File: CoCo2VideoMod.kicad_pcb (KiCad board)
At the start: 2 copper layers, 38 x 50 mm, 36 parts, among them J1 20261043, J2 to PCB, J3 Video, Q1 BC547, Q2 BC557, Q3 BC547, Q4 BC557, Q5 BC547, U1 MC1372P

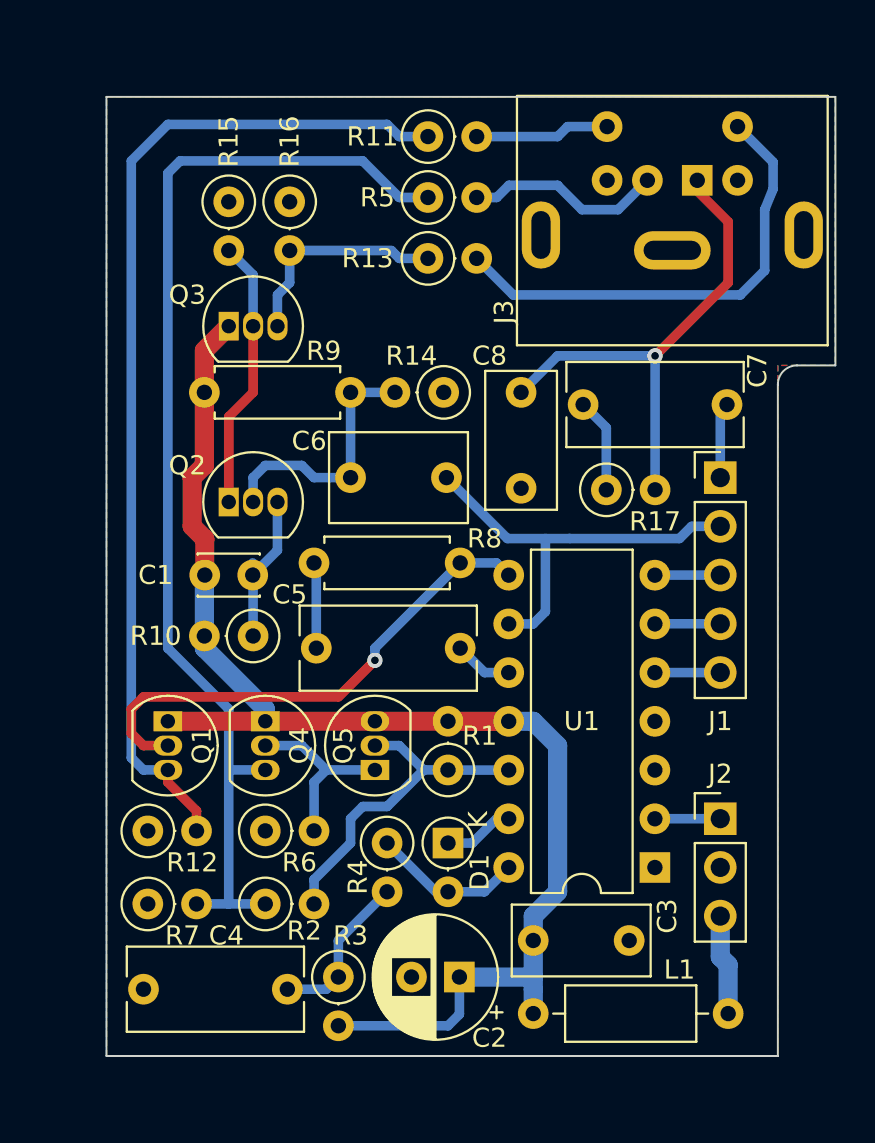
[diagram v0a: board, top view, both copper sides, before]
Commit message: increased distance components to PCB edge
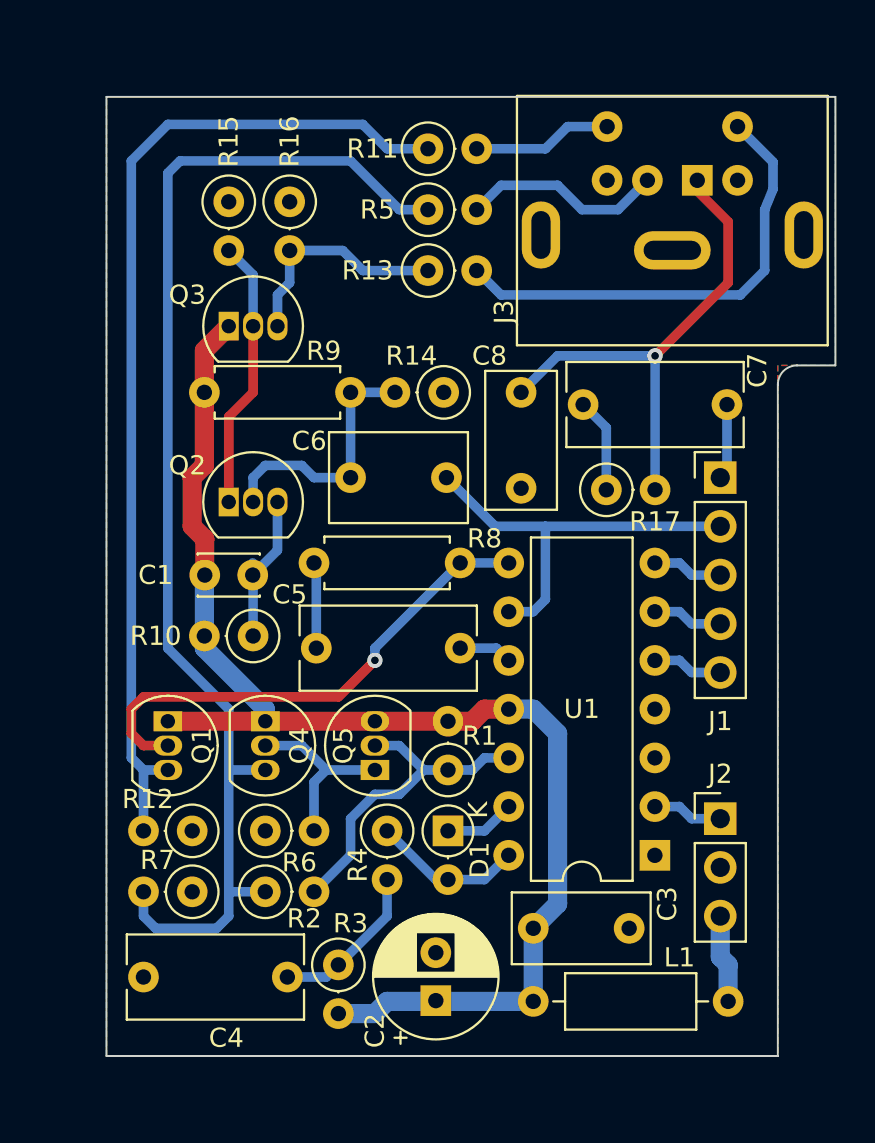
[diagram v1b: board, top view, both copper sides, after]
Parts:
- moved R7 2.40 mm to (204.5, 91.4), turned to 180 degrees
- moved R12 2.31 mm to (204.5, 88.3), turned to 180 degrees
- moved C2 1.74 mm to (217.2, 97.1), turned to 90 degrees
- moved C3 0.64 mm to (222.2, 93.3)
- moved D1 0.64 mm to (217.8, 88.3)
- moved L1 0.64 mm to (232.4, 97.2)
- moved R2 0.64 mm to (208.3, 91.4)
- moved R3 0.64 mm to (212.1, 95.2)
- moved R4 0.64 mm to (214.6, 88.3)
- moved R5 0.64 mm to (216.8, 55.9)
- moved R11 0.63 mm to (216.8, 52.7)
- moved R13 0.63 mm to (216.8, 59.1)
- moved C4 0.63 mm to (201.9, 95.9)
- moved U1 0.63 mm to (228.6, 89.5)
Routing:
- net Net-(Q5-E): track 59.5 -> 65.0 mm
- net +5V: track 70.7 -> 69.0 mm
- net /+5V in: track 5.25 -> 4.61 mm
- net /Luma: track 21.8 -> 21.3 mm

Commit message: production files JLC, production complete
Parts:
- moved J3 1.30 mm to (229.5, 54.4)

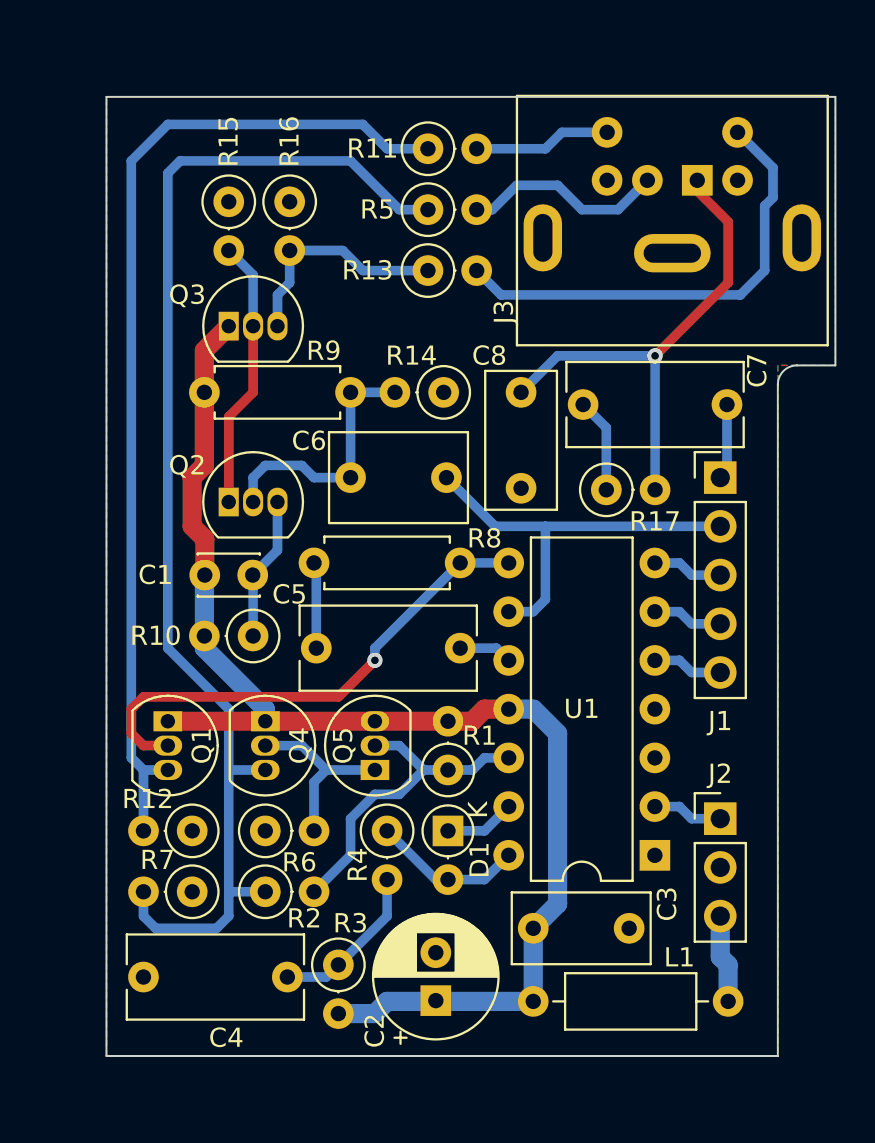
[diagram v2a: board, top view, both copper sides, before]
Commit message: rotated connector, added GND pins
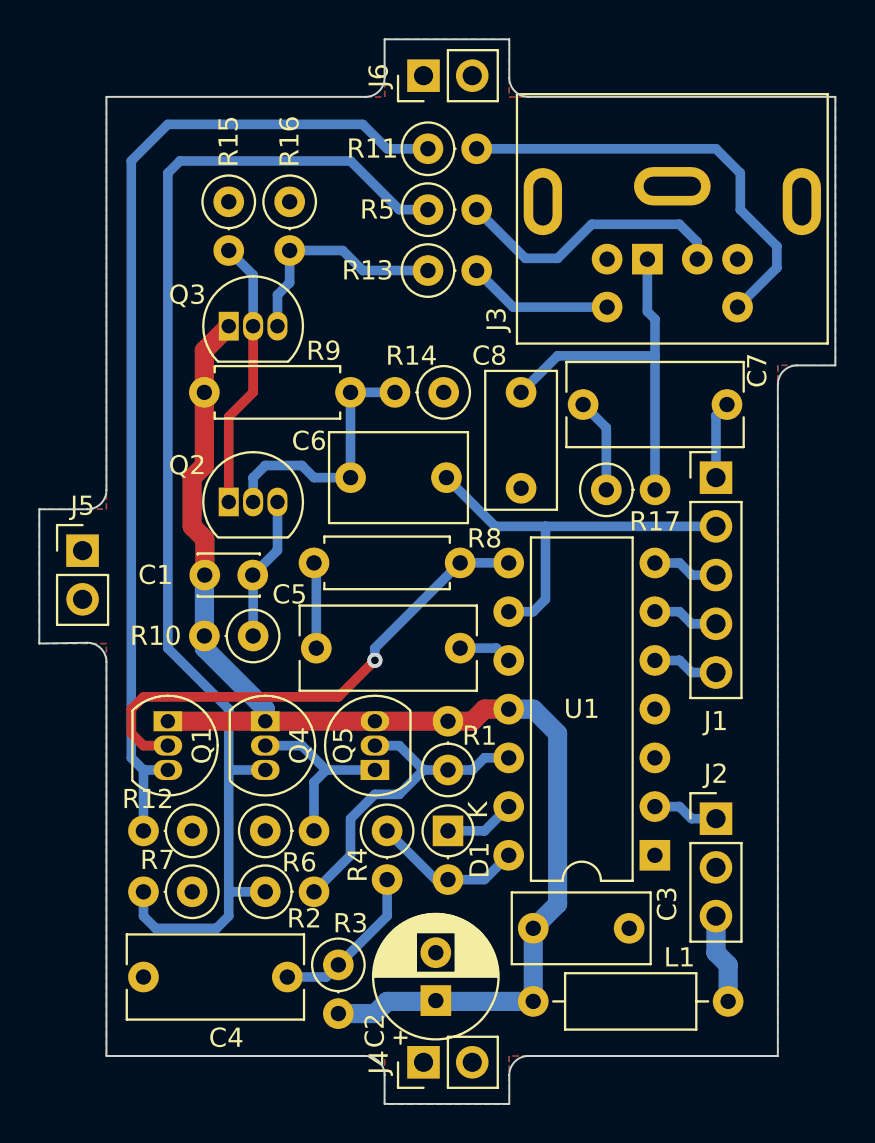
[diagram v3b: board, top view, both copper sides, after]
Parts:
- added J4: GND_S, Connector_PinHeader_2.54mm:PinHeader_1x02_P2.54mm_Vertical, F.Cu at (216.5, 100.3)
- added J5: GND_W, Connector_PinHeader_2.54mm:PinHeader_1x02_P2.54mm_Vertical, F.Cu at (198.8, 73.7)
- added J6: GND_N, Connector_PinHeader_2.54mm:PinHeader_1x02_P2.54mm_Vertical, F.Cu at (216.5, 48.9)
- moved J3 4.11 mm to (229.5, 58.5), turned to 180 degrees
- moved J1 0.22 mm to (231.8, 69.8)
- moved J2 0.22 mm to (231.8, 87.6)
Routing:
- net /Luma_out: track 24.2 -> 7.59 mm
- net /Chroma_out: track 7.15 -> 22.9 mm
- net /Audio out: track 26.7 -> 20.0 mm, vias 1 -> 0
- net /Composite_out: track 10.6 -> 14.6 mm
- net GND: track 2.11 -> 1.11 mm
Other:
- board size 38 x 50 mm -> 41.5 x 55.5 mm

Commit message: adjusted GND pin position, added PCB description to silk screen, started README
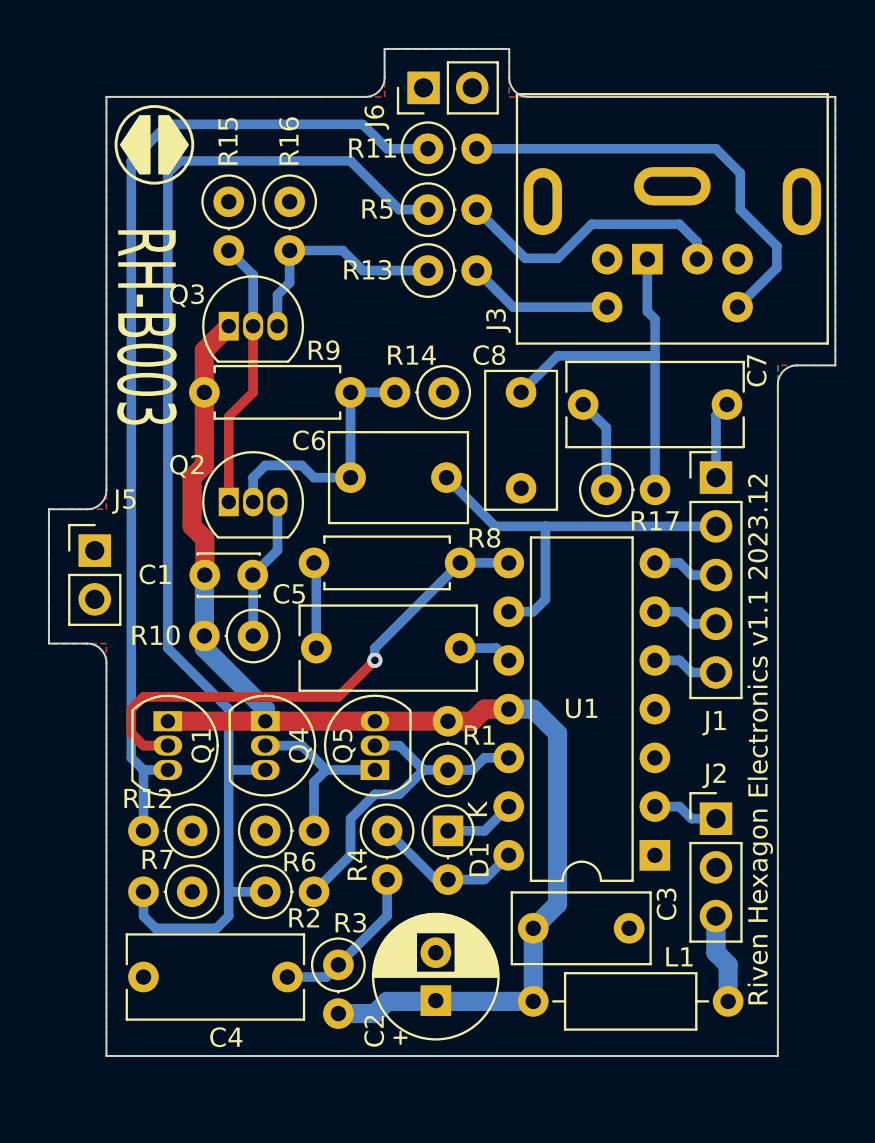
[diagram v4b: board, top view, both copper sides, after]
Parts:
- removed J4: GND_S, Connector_PinHeader_2.54mm:PinHeader_1x02_P2.54mm_Vertical
- moved J6 0.63 mm to (216.5, 49.5)
- moved J5 0.63 mm to (199.4, 73.7)
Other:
- board size 41.5 x 55.5 mm -> 41 x 52.5 mm
- board text added: "RH-B003"
- board text added: "Riven Hexagon Electronics v1.1 2023.12"
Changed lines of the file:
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@@
   )
   (footprint "Connector_PinHeader_2.54mm:PinHeader_1x02_P2.54mm_Vertical" (layer "F.Cu")
-    (at 216.53 48.895 90)
+    (at 216.53 49.53 90)
     (descr "Through hole straight pin header, 1x02, 2.54mm pitch, single row")
     (tags "Through hole pin header THT 1x02 2.54mm single row")
@@
     (property "ki_keywords" "connector")
     (attr through_hole)
-    (fp_text reference "J6" (at 0 -2.33 90) (layer "F.SilkS")
+    (fp_text reference "J6" (at -1.47 -2.53 90) (layer "F.SilkS")
         (effects (font (size 1 1) (thickness 0.15)))
     )
@@
       (net 3 "GND") (pintype "passive"))
     (model "${KICAD6_3DMODEL_DIR}/Capacitor_THT.3dshapes/CP_Radial_D6.3mm_P2.50mm.wrl"
-      (offset (xyz 0 0 0))
-      (scale (xyz 1 1 1))
-      (rotate (xyz 0 0 0))
-    )
-  )
-  (footprint "Connector_PinHeader_2.54mm:PinHeader_1x02_P2.54mm_Vertical" (layer "F.Cu")
-    (at 216.53 100.33 90)
-    (descr "Through hole straight pin header, 1x02, 2.54mm pitch, single row")
-    (tags "Through hole pin header THT 1x02 2.54mm single row")
-    (property "Sheetfile" "CoCo2VideoMod.kicad_sch")
-    (property "Sheetname" "")
-    (property "ki_description" "Generic connector, single row, 01x02, script generated (kicad-library-utils/schlib/autogen/connector/)")
-    (property "ki_keywords" "connector")
-    (attr through_hole)
-    (fp_text reference "J4" (at 0 -2.33 90) (layer "F.SilkS")
-        (effects (font (size 1 1) (thickness 0.15)))
-    )
-    (fp_text value "GND_S" (at 0 4.87 90) (layer "F.Fab")
-        (effects (font (size 1 1) (thickness 0.15)))
-    )
-    (fp_text user "${REFERENCE}" (at 0 1.27) (layer "F.Fab")
-        (effects (font (size 1 1) (thickness 0.15)))
-    )
-    (fp_line (start -1.33 -1.33) (end 0 -1.33)
-      (stroke (width 0.12) (type solid)) (layer "F.SilkS"))
-    (fp_line (start -1.33 0) (end -1.33 -1.33)
-      (stroke (width 0.12) (type solid)) (layer "F.SilkS"))
-    (fp_line (start -1.33 1.27) (end -1.33 3.87)
-      (stroke (width 0.12) (type solid)) (layer "F.SilkS"))
-    (fp_line (start -1.33 1.27) (end 1.33 1.27)
-      (stroke (width 0.12) (type solid)) (layer "F.SilkS"))
-    (fp_line (start -1.33 3.87) (end 1.33 3.87)
-      (stroke (width 0.12) (type solid)) (layer "F.SilkS"))
-    (fp_line (start 1.33 1.27) (end 1.33 3.87)
-      (stroke (width 0.12) (type solid)) (layer "F.SilkS"))
-    (fp_line (start -1.8 -1.8) (end -1.8 4.35)
-      (stroke (width 0.05) (type solid)) (layer "F.CrtYd"))
-    (fp_line (start -1.8 4.35) (end 1.8 4.35)
-      (stroke (width 0.05) (type solid)) (layer "F.CrtYd"))
-    (fp_line (start 1.8 -1.8) (end -1.8 -1.8)
-      (stroke (width 0.05) (type solid)) (layer "F.CrtYd"))
-    (fp_line (start 1.8 4.35) (end 1.8 -1.8)
-      (stroke (width 0.05) (type solid)) (layer "F.CrtYd"))
-    (fp_line (start -1.27 -0.635) (end -0.635 -1.27)
-      (stroke (width 0.1) (type solid)) (layer "F.Fab"))
-    (fp_line (start -1.27 3.81) (end -1.27 -0.635)
-      (stroke (width 0.1) (type solid)) (layer "F.Fab"))
-    (fp_line (start -0.635 -1.27) (end 1.27 -1.27)
-      (stroke (width 0.1) (type solid)) (layer "F.Fab"))
-    (fp_line (start 1.27 -1.27) (end 1.27 3.81)
-      (stroke (width 0.1) (type solid)) (layer "F.Fab"))
-    (fp_line (start 1.27 3.81) (end -1.27 3.81)
-      (stroke (width 0.1) (type solid)) (layer "F.Fab"))
-    (pad "1" thru_hole rect (at 0 0 90) (size 1.7 1.7) (drill 1) (layers "*.Cu" "*.Mask")
-      (net 3 "GND") (pinfunction "Pin_1") (pintype "passive"))
-    (pad "2" thru_hole oval (at 0 2.54 90) (size 1.7 1.7) (drill 1) (layers "*.Cu" "*.Mask")
-      (net 3 "GND") (pinfunction "Pin_2") (pintype "passive"))
-    (model "${KICAD6_3DMODEL_DIR}/Connector_PinHeader_2.54mm.3dshapes/PinHeader_1x02_P2.54mm_Vertical.wrl"
       (offset (xyz 0 0 0))
       (scale (xyz 1 1 1))
@@
   )
   (footprint "Connector_PinHeader_2.54mm:PinHeader_1x02_P2.54mm_Vertical" (layer "F.Cu")
-    (at 198.755 73.655)
+    (at 199.39 73.655)
     (descr "Through hole straight pin header, 1x02, 2.54mm pitch, single row")
     (tags "Through hole pin header THT 1x02 2.54mm single row")
@@
     (property "ki_keywords" "connector")
     (attr through_hole)
-    (fp_text reference "J5" (at 0 -2.33) (layer "F.SilkS")
+    (fp_text reference "J5" (at 1.61 -2.655) (layer "F.SilkS")
         (effects (font (size 1 1) (thickness 0.15)))
     )
@@
     )
   )
-  (gr_line (start 196.5 71.5) (end 196.5 78.5)
+  (gr_poly
+    (pts
+      (xy 201.75 54)
+      (xy 200.75 52.5)
+      (xy 201.75 51)
+      (xy 202.25 51)
+      (xy 202.25 54)
+    )
+    (stroke (width 0.1) (type solid)) (fill solid) (layer "F.SilkS"))
+  (gr_circle (center 202.5 52.5) (end 202.5 54.5)
+    (stroke (width 0.15) (type solid)) (fill none) (layer "F.SilkS"))
+  (gr_poly
+    (pts
+      (xy 203.25 54)
+      (xy 202.75 54)
+      (xy 202.75 51)
+      (xy 203.25 51)
+      (xy 204.25 52.5)
+    )
+    (stroke (width 0.1) (type solid)) (fill solid) (layer "F.SilkS"))
+  (gr_line (start 197 71.5) (end 197 78.5)
     (stroke (width 0.1) (type default)) (layer "Edge.Cuts"))
-  (gr_line (start 221.000001 47) (end 221.000001 48.999999)
+  (gr_line (start 221.000001 47.5) (end 221.000001 49)
     (stroke (width 0.1) (type default)) (layer "Edge.Cuts"))
-  (gr_line (start 200 100) (end 200 79.457107)
-    (stroke (width 0.1) (type default)) (layer "Edge.Cuts"))
-  (gr_arc (start 221 101) (mid 221.292893 100.292893) (end 222 100)
-    (stroke (width 0.1) (type default)) (layer "Edge.Cuts"))
-  (gr_line (start 221 102.5) (end 214.5 102.5)
+  (gr_line (start 200 100) (end 200 79.500007)
     (stroke (width 0.1) (type default)) (layer "Edge.Cuts"))
   (gr_line (start 238 50) (end 222.000001 49.999999)
     (stroke (width 0.1) (type default)) (layer "Edge.Cuts"))
-  (gr_arc (start 199 78.457107) (mid 199.707107 78.75) (end 200 79.457107)
+  (gr_arc (start 222.000001 49.999999) (mid 221.292894 49.707106) (end 221.000001 49)
     (stroke (width 0.1) (type default)) (layer "Edge.Cuts"))
-  (gr_line (start 196.5 78.5) (end 199 78.457107)
+  (gr_line (start 197 78.5) (end 199 78.500007)
     (stroke (width 0.1) (type default)) (layer "Edge.Cuts"))
-  (gr_line (start 214.5 49) (end 214.5 47)
+  (gr_line (start 214.5 49) (end 214.5 47.5)
+    (stroke (width 0.1) (type default)) (layer "Edge.Cuts"))
+  (gr_arc (start 199 78.500007) (mid 199.707104 78.792901) (end 199.999993 79.500007)
     (stroke (width 0.1) (type default)) (layer "Edge.Cuts"))
   (gr_arc (start 235 65) (mid 235.292893 64.292893) (end 236 64)
@@
   (gr_line (start 236 64) (end 238 64)
     (stroke (width 0.1) (type default)) (layer "Edge.Cuts"))
-  (gr_arc (start 213.5 100) (mid 214.207107 100.292893) (end 214.5 101)
+  (gr_line (start 199 71.5) (end 197 71.5)
     (stroke (width 0.1) (type default)) (layer "Edge.Cuts"))
-  (gr_line (start 199 71.5) (end 196.5 71.5)
+  (gr_line (start 235 100) (end 200 100)
     (stroke (width 0.1) (type default)) (layer "Edge.Cuts"))
-  (gr_line (start 235 100) (end 222 100)
+  (gr_line (start 238 64) (end 238 50)
+    (stroke (width 0.1) (type default)) (layer "Edge.Cuts"))
+  (gr_arc (start 200 70.5) (mid 199.707107 71.207107) (end 199 71.5)
     (stroke (width 0.1) (type default)) (layer "Edge.Cuts"))
   (gr_arc (start 214.5 49) (mid 214.207107 49.707107) (end 213.5 50)
     (stroke (width 0.1) (type default)) (layer "Edge.Cuts"))
-  (gr_line (start 214.5 102.5) (end 214.5 101)
-    (stroke (width 0.1) (type default)) (layer "Edge.Cuts"))
-  (gr_line (start 213.5 100) (end 200 100)
-    (stroke (width 0.1) (type default)) (layer "Edge.Cuts"))
-  (gr_line (start 238 64) (end 238 50)
-    (stroke (width 0.1) (type default)) (layer "Edge.Cuts"))
-  (gr_arc (start 222.000001 49.999999) (mid 221.292894 49.707106) (end 221.000001 48.999999)
-    (stroke (width 0.1) (type default)) (layer "Edge.Cuts"))
-  (gr_arc (start 200 70.5) (mid 199.707107 71.207107) (end 199 71.5)
-    (stroke (width 0.1) (type default)) (layer "Edge.Cuts"))
   (gr_line (start 200 50) (end 213.5 50)
     (stroke (width 0.1) (type default)) (layer "Edge.Cuts"))
-  (gr_line (start 221 101) (end 221 102.5)
-    (stroke (width 0.1) (type default)) (layer "Edge.Cuts"))
-  (gr_line (start 214.5 47) (end 221.000001 47)
+  (gr_line (start 214.5 47.5) (end 221.000001 47.5)
     (stroke (width 0.1) (type default)) (layer "Edge.Cuts"))
   (gr_line (start 200 70.5) (end 200 50)
@@
   (gr_line (start 235 100) (end 235 65)
     (stroke (width 0.1) (type default)) (layer "Edge.Cuts"))
+  (gr_text "RH-B003" (at 202 62 270) (layer "F.SilkS")
+    (effects (font (size 3 1.75) (thickness 0.3)))
+  )
+  (gr_text "Riven Hexagon Electronics v1.1 2023.12" (at 234 83.5 90) (layer "F.SilkS")
+    (effects (font (size 1 1) (thickness 0.15)))
+  )
   (gr_text "K" (at 219.964 87.63 90) (layer "F.SilkS")
     (effects (font (size 1 1) (thickness 0.15)) (justify left bottom))
@@
       (pts
         (xy 200 78.5)
-        (xy 196.5 78.5)
-        (xy 196.5 71.5)
+        (xy 197 78.5)
+        (xy 197 71.5)
         (xy 200 71.5)
         (xy 200 50)
         (xy 214.5 50)
-        (xy 214.5 47)
-        (xy 221 47)
+        (xy 214.5 47.5)
+        (xy 221 47.5)
         (xy 221 50)
         (xy 238 50)
@@
         (xy 235 64)
         (xy 235 100)
-        (xy 221 100)
-        (xy 221 102.5)
-        (xy 214.5 102.5)
-        (xy 214.5 100)
         (xy 200 100)
       )
@@
       (pts
         (xy 200 78.5)
-        (xy 196.5 78.5)
-        (xy 196.5 71.5)
+        (xy 197 78.5)
+        (xy 197 71.5)
         (xy 200 71.5)
         (xy 200 50)
         (xy 214.5 50)
-        (xy 214.5 47)
-        (xy 221 47)
+        (xy 214.5 47.5)
+        (xy 221 47.5)
         (xy 221 50)
         (xy 238 50)
@@
         (xy 235 64)
         (xy 235 100)
-        (xy 221 100)
-        (xy 221 102.5)
-        (xy 214.5 102.5)
-        (xy 214.5 100)
         (xy 200 100)
       )
